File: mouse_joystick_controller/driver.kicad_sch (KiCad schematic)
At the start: 13 parts, among them J4 Conn_FFC_20_Pin_1mm_bottom-ZF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, U6 LVDS_4-4_HALF_DS91M040TSQE, U7 LVDS_4-4_HALF_DS91M040TSQE

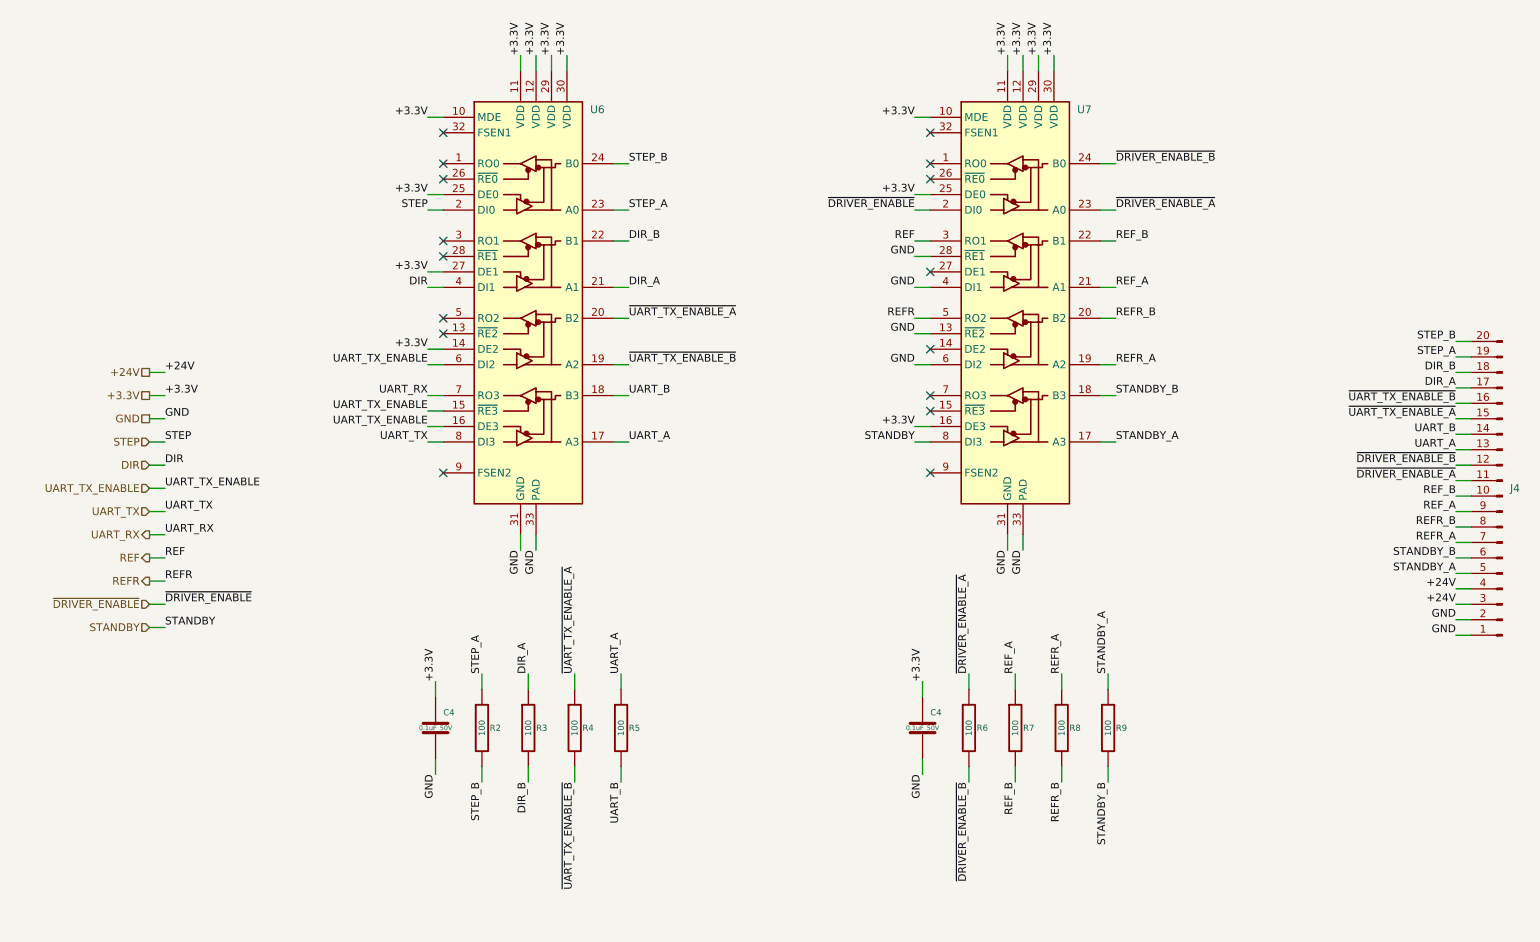
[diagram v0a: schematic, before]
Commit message: Move standby pin
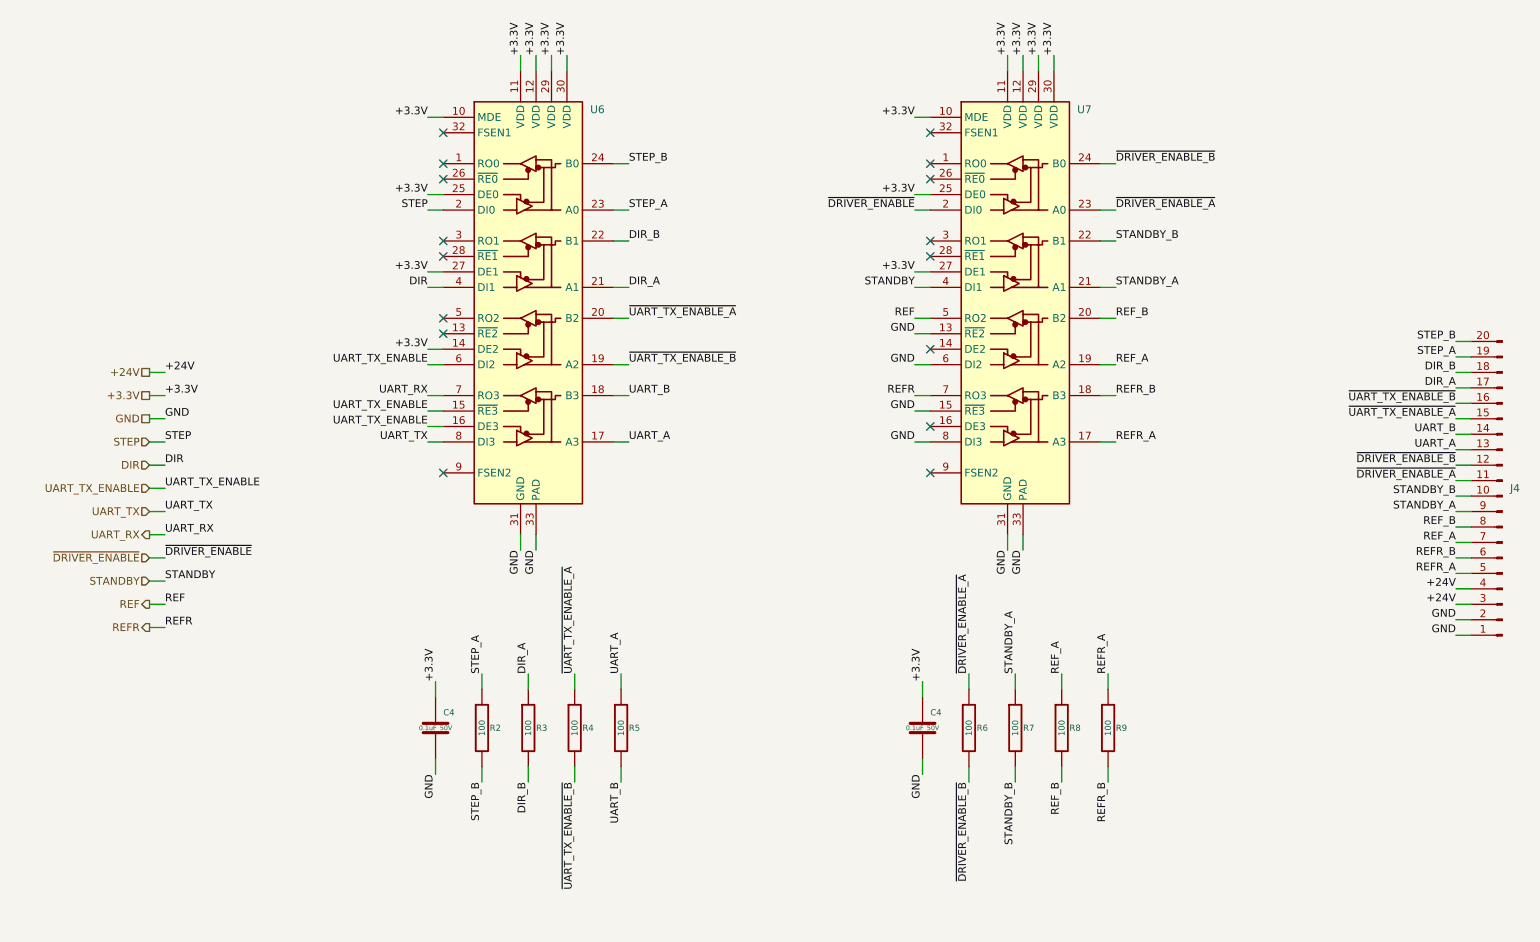
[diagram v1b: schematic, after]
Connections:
- net +3.3V: now also U7.27 (DE1); no longer U7.16 (DE3)
- net GND: now also U7.15 (~{RE3}), U7.8 (DI3); no longer U7.28 (~{RE1}), U7.4 (DI1)
- net REF: now also U7.5 (RO2); no longer U7.3 (RO1)
- net REFR: now also U7.7 (RO3); no longer U7.5 (RO2)
- net REFR_A: now also J4.5 (Pin_5), R9.1, U7.17 (A3); no longer J4.7 (Pin_7), R8.1, U7.19 (A2)
- net REFR_B: now also J4.6 (Pin_6), R9.2, U7.18 (B3); no longer J4.8 (Pin_8), R8.2, U7.20 (B2)
- net REF_A: now also J4.7 (Pin_7), R8.1, U7.19 (A2); no longer J4.9 (Pin_9), R7.1, U7.21 (A1)
- net REF_B: now also J4.8 (Pin_8), R8.2, U7.20 (B2); no longer J4.10 (Pin_10), R7.2, U7.22 (B1)
- net STANDBY: now also U7.4 (DI1); no longer U7.8 (DI3)
- net STANDBY_A: now also J4.9 (Pin_9), R7.1, U7.21 (A1); no longer J4.5 (Pin_5), R9.1, U7.17 (A3)
- net STANDBY_B: now also J4.10 (Pin_10), R7.2, U7.22 (B1); no longer J4.6 (Pin_6), R9.2, U7.18 (B3)
